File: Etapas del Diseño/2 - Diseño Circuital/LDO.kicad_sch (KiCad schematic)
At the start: 54 parts, among them J1 Vo, J2 V_Rs_test, J3 V_current_test, J4 V_voltage_test, J5 V_ref_test, J6 V_ref_c_test, Q1 2N3904, Q10 BC557, Q11 BC547, Q12 BC557, Q13 2N3906, Q14 2N3904, Q15 2N3906, Q16 2N3904, Q17 2N3906, Q18 2N3904, Q19 2N3904, Q2 2N3904, Q3 2N3904, Q4 2N3906, Q5 2N3906, Q6 2N3904, Q7 2N3904, Q8 IRF4905, Q9 BC547, U1 TL431LP, U2 LM358, U4 LM358, U5 LM358, U6 LM358

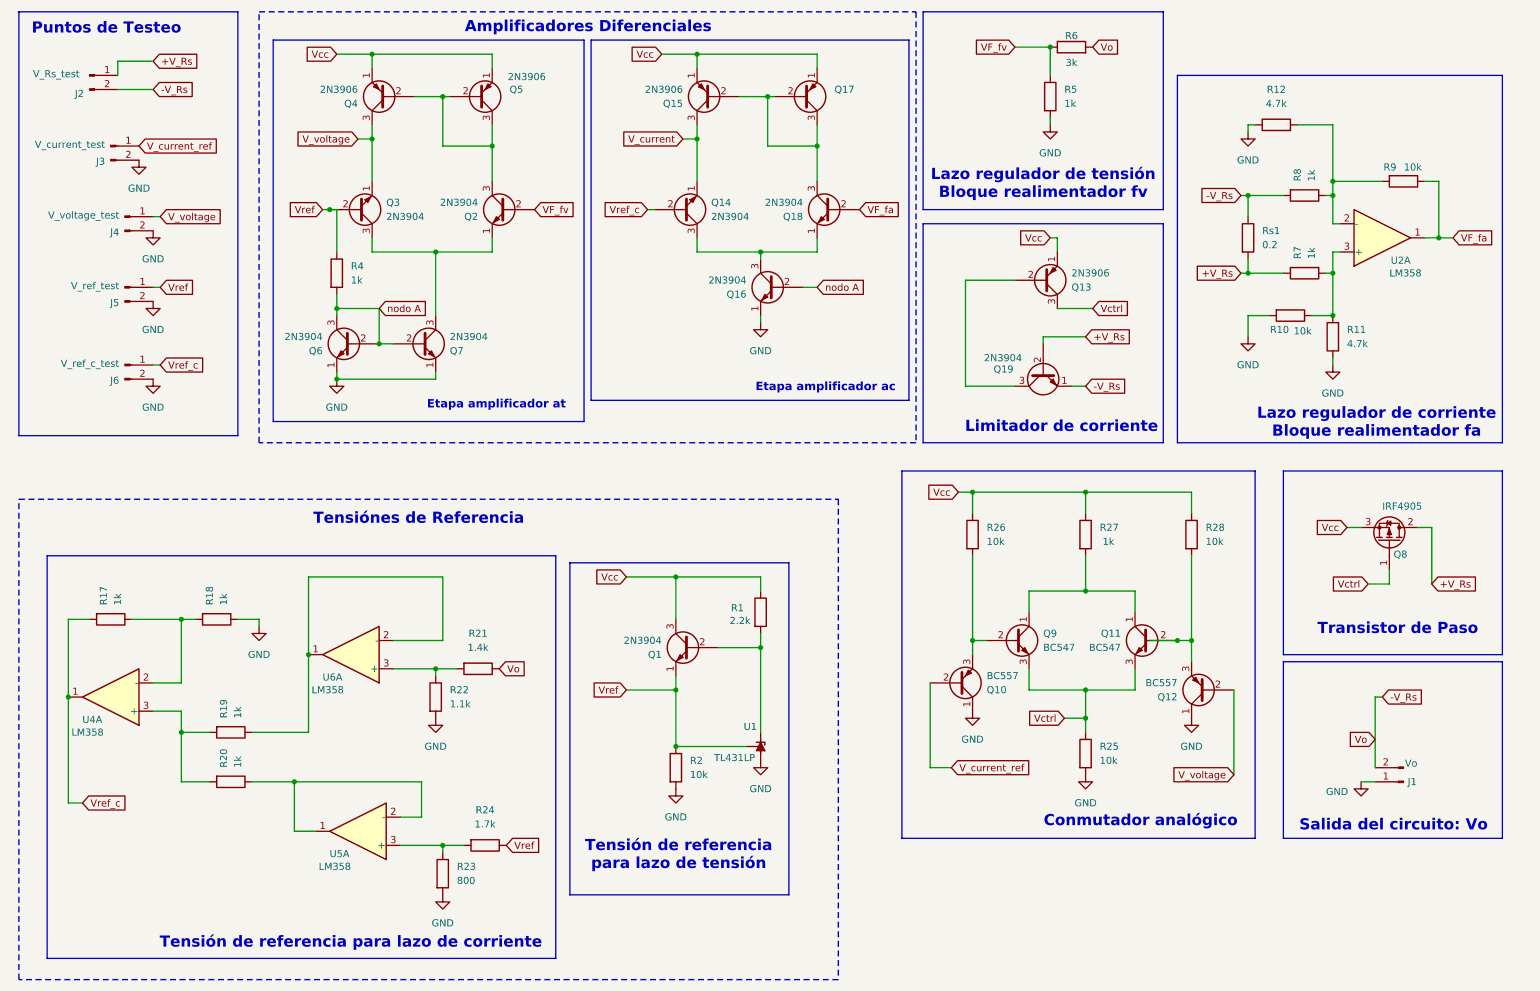
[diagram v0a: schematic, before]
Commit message: Arreglo pares diferenciales en el esquematico
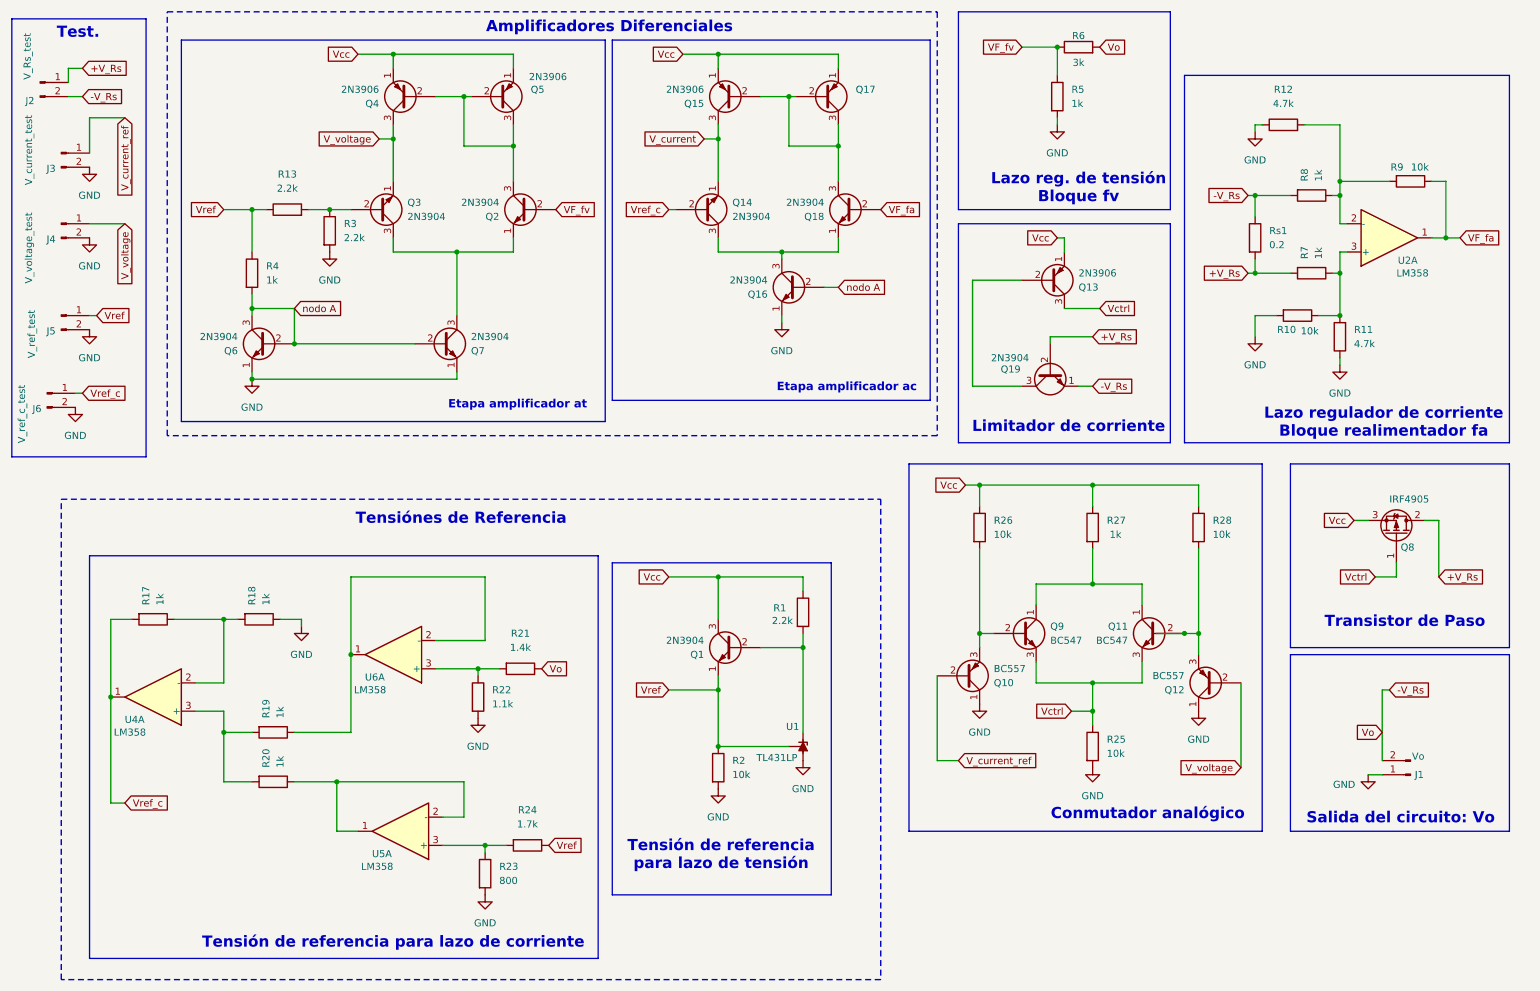
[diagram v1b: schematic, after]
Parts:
- added R13, R3: 2.2k, symbol Device:R
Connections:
- net GND: now also R3.2
- net Vref: now also R13.1; no longer Q3.2 (B)
- new net: Q3.2 (B), R13.2, R3.1
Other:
- note added: "Lazo reg. de tensión Bloque fv"
- note added: "Test."
- note removed: "Lazo regulador de tensión Bloque realimentador fv"
- note removed: "Puntos de Testeo"
- moved on the sheet: J1, J2, J3, J4, J5, J6, Q1, Q10, Q11, Q12, Q13, Q14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
